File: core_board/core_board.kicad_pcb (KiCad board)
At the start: 2 copper layers, 27 x 60 mm, 36 parts, among them J1 Conn_01x13_Socket, J2 Conn_01x13_Socket, J3 Ignitor Output, J4 Micro_SD_Card, J5 Battery Input, J7 Connector 1, J8 Connector 2, U1 CPC1002N, U2 CPC1002N, U3 CPC1002N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

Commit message: Fixed connector compatibility with STEMMA QT and Qwiic
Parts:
- J7, J8: footprint Connector_Molex:Molex_PicoBlade_53047-0410_1x04_P1.25mm_Vertical -> G2Custom:JST_SH_BM04B-SRSS-TB_1x04-1MP_P1.00mm_Vertical-CUSTOM
- moved J7 1.46 mm to (118.8, 74.5)
- moved J8 0.98 mm to (118.8, 82.5)
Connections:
- J7 pad 1: +3.3V -> /SCL Inter Board
- J7 pad 2: /SCL Inter Board -> /SDA Inter Board
- J7 pad 3: /SDA Inter Board -> +3.3V
- J8 pad 1: +3.3V -> /SCL Inter Board
- J8 pad 2: /SCL Inter Board -> /SDA Inter Board
- J8 pad 3: /SDA Inter Board -> +3.3V
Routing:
- net +3.3V: track 117.7 -> 106.2 mm
- net /SDA Inter Board: track 22.2 -> 24.6 mm, vias 0 -> 2
- net GND: track 20.0 -> 21.5 mm, vias 19 -> 21
- net /SCL Inter Board: track 21.5 -> 22.0 mm

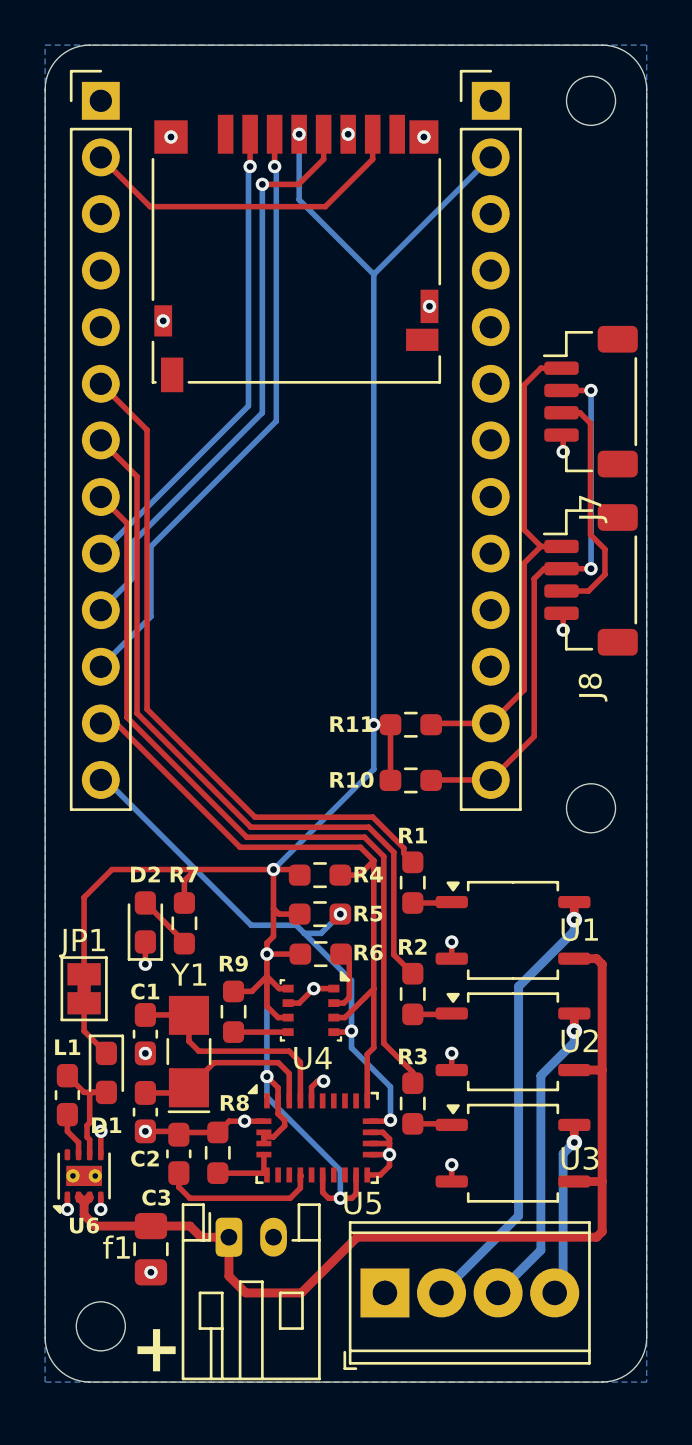
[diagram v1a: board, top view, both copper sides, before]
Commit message: Corrected DRC errors
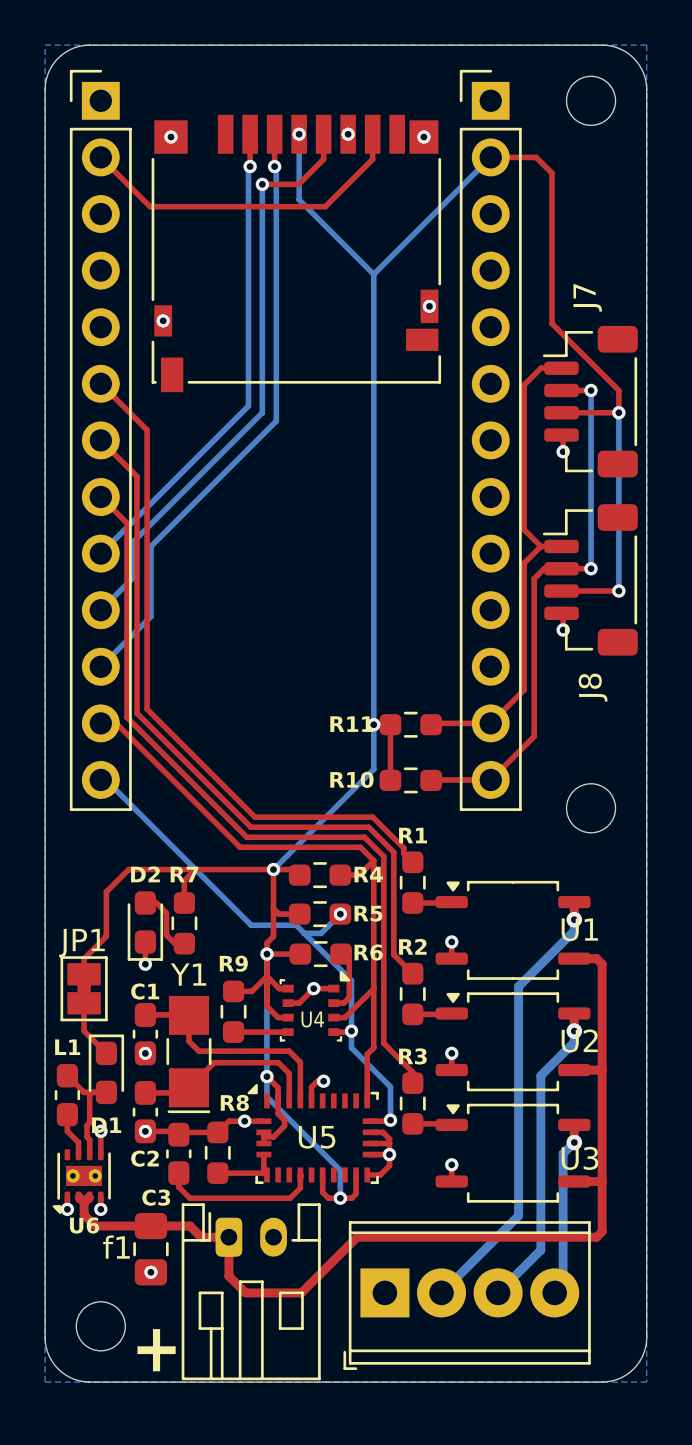
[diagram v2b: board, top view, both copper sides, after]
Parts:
- Y1: value 33.768kHz -> 32.768kHz
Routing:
- net +3.3V: track 106.2 -> 123.1 mm, vias 6 -> 8
- net Net-(D2-A): track 2.55 -> 3.09 mm
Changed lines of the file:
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@@
 			)
 		)
-		(property "Value" "33.768kHz"
+		(property "Value" "32.768kHz"
 			(at 0 -2 90)
 			(layer "F.Fab")
@@
 		(tags "lga land grid array")
 		(property "Reference" "U4"
-			(at 2.18125 -0.06875 180)
+			(at 0.43125 -0.06875 180)
 			(layer "F.SilkS")
 			(effects
 				(font
-					(size 1 1)
-					(thickness 0.15)
+					(size 0.7 0.6)
+					(thickness 0.125)
 				)
 			)
@@
 		(tags "LGA 28 5.2x3.8mm Pitch 0.5mm")
 		(property "Reference" "U5"
-			(at 2.04375 2.95625 0)
+			(at 0 0 0)
 			(layer "F.SilkS")
 			(effects
@@
 		(tags "connector JST SH vertical")
 		(property "Reference" "J7"
-			(at 4.75 0 90)
+			(at -4.75 0.25 90)
 			(layer "F.SilkS")
 			(effects
@@
 	)
 	(segment
-		(start 118.725 75.475)
-		(end 118.25 75)
-		(width 0.25)
-		(layer "F.Cu")
-		(net 1)
-	)
-	(segment
-		(start 118.725 80.475)
-		(end 118.725 75.475)
+		(start 100.5 96)
+		(end 101 95.5)
 		(width 0.25)
 		(layer "F.Cu")
@@
 	)
 	(segment
-		(start 97.25 95.5)
-		(end 99.922924 95.5)
+		(start 104.20625 101.64375)
+		(end 104.20625 100.29375)
 		(width 0.25)
 		(layer "F.Cu")
@@
 	)
 	(segment
-		(start 100.5 96)
-		(end 101 95.5)
+		(start 108.0135 110.25)
+		(end 108.20625 110.05725)
 		(width 0.25)
 		(layer "F.Cu")
@@
 	)
 	(segment
-		(start 104.20625 101.64375)
-		(end 104.20625 100.29375)
+		(start 114.25 63.54)
+		(end 116.29 63.54)
 		(width 0.25)
 		(layer "F.Cu")
@@
 	)
 	(segment
-		(start 108.0135 110.25)
-		(end 108.20625 110.05725)
+		(start 117 64.25)
+		(end 117 71)
 		(width 0.25)
 		(layer "F.Cu")
@@
 	)
 	(segment
-		(start 96 96.75)
-		(end 97.25 95.5)
+		(start 117 71)
+		(end 120 74)
 		(width 0.25)
 		(layer "F.Cu")
@@
 	)
 	(segment
-		(start 96 100.2)
-		(end 96 96.75)
-		(width 0.25)
-		(layer "F.Cu")
-		(net 1)
-	)
-	(segment
 		(start 104.20625 101.64375)
 		(end 104.70625 102.14375)
@@
 	)
 	(segment
+		(start 98 95.5)
+		(end 101 95.5)
+		(width 0.25)
+		(layer "F.Cu")
+		(net 1)
+	)
+	(segment
 		(start 105.70625 99.29375)
 		(end 104.20625 99.29375)
@@
 	)
 	(segment
-		(start 118.633884 83)
-		(end 119.375 82.258884)
+		(start 97 98.5)
+		(end 97 96.5)
 		(width 0.25)
 		(layer "F.Cu")
@@
 	)
 	(segment
-		(start 119.375 81.125)
-		(end 118.725 80.475)
+		(start 120 74)
+		(end 120 75)
 		(width 0.25)
 		(layer "F.Cu")
@@
 	)
 	(segment
+		(start 96 100.2)
+		(end 96 99.5)
+		(width 0.25)
+		(layer "F.Cu")
+		(net 1)
+	)
+	(segment
 		(start 105 106.7625)
 		(end 105 107)
@@
 	)
 	(segment
+		(start 117.425 75)
+		(end 120 75)
+		(width 0.25)
+		(layer "F.Cu")
+		(net 1)
+	)
+	(segment
 		(start 104.5 98.5)
 		(end 104.20625 98.79375)
@@
 	)
 	(segment
-		(start 117.425 83)
-		(end 118.633884 83)
+		(start 96 99.5)
+		(end 97 98.5)
 		(width 0.25)
 		(layer "F.Cu")
@@
 	)
 	(segment
+		(start 116.29 63.54)
+		(end 117 64.25)
+		(width 0.25)
+		(layer "F.Cu")
+		(net 1)
+	)
+	(segment
 		(start 104.70625 105.29375)
 		(end 104.20625 104.79375)
@@
 	)
 	(segment
-		(start 119.375 82.258884)
-		(end 119.375 81.125)
+		(start 104.06875 107.29375)
+		(end 104.06875 107.5)
 		(width 0.25)
 		(layer "F.Cu")
@@
 	)
 	(segment
-		(start 104.06875 107.29375)
-		(end 104.06875 107.5)
+		(start 117.425 83)
+		(end 120 83)
 		(width 0.25)
 		(layer "F.Cu")
@@
 	)
 	(segment
-		(start 99.922924 95.5)
-		(end 101 95.5)
+		(start 97 96.5)
+		(end 98 95.5)
 		(width 0.25)
 		(layer "F.Cu")
@@
 		(net 1)
 	)
-	(segment
-		(start 118.25 75)
-		(end 117.425 75)
-		(width 0.25)
-		(layer "F.Cu")
+	(via
+		(at 120 75)
+		(size 0.6)
+		(drill 0.3)
+		(layers "F.Cu" "B.Cu")
 		(net 1)
 	)
@@
 		(net 1)
 	)
+	(via
+		(at 120 83)
+		(size 0.6)
+		(drill 0.3)
+		(layers "F.Cu" "B.Cu")
+		(net 1)
+	)
 	(segment
 		(start 107.5 109)
@@
 	)
 	(segment
+		(start 120 83)
+		(end 120 75)
+		(width 0.25)
+		(layer "B.Cu")
+		(net 1)
+	)
+	(segment
 		(start 104.5 95.5)
 		(end 109 91)
@@
 	)
 	(segment
-		(start 100.5 98.75)
-		(end 100.5 98.825)
+		(start 99.7 97.45)
+		(end 99.7 98.45)
 		(width 0.25)
 		(layer "F.Cu")
@@
 	(segment
 		(start 98.75 97)
-		(end 100.5 98.75)
+		(end 99.25 97)
+		(width 0.25)
+		(layer "F.Cu")
+		(net 48)
+	)
+	(segment
+		(start 100.075 98.825)
+		(end 100.5 98.825)
+		(width 0.25)
+		(layer "F.Cu")
+		(net 48)
+	)
+	(segment
+		(start 99.25 97)
+		(end 99.7 97.45)
+		(width 0.25)
+		(layer "F.Cu")
+		(net 48)
+	)
+	(segment
+		(start 99.7 98.45)
+		(end 100.075 98.825)
 		(width 0.25)
 		(layer "F.Cu")
@@
 	)
 	(zone
+		(net 46)
+		(net_name "GND")
+		(layer "F.Cu")
+		(name "$teardrop_padvia$")
+		(hatch full 0.1)
+		(priority 30001)
+		(attr
+			(teardrop
+				(type padvia)
+			)
+		)
+		(connect_pads yes
+			(clearance 0)
+		)
+		(min_thickness 0.0254)
+		(filled_areas_thickness no)
+		(fill yes
+			(thermal_gap 0.5)
+			(thermal_bridge_width 0.5)
+			(island_removal_mode 1)
+			(island_area_min 10)
+		)
+		(polygon
+			(pts
+				(xy 96.875 110.2) (xy 96.625 110.2) (xy 96.472836 110.635195) (xy 96.75 110.751) (xy 97.027164 110.635195)
+			)
+		)
+	)
+	(zone
+		(net 46)
+		(net_name "GND")
+		(layer "F.Cu")
+		(name "$teardrop_padvia$")
+		(hatch full 0.1)
+		(priority 30002)
+		(attr
+			(teardrop
+				(type padvia)
+			)
+		)
+		(connect_pads yes
+			(clearance 0)
+		)
+		(min_thickness 0.0254)
+		(filled_areas_thickness no)
+		(fill yes
+			(thermal_gap 0.5)
+			(thermal_bridge_width 0.5)
+			(island_removal_mode 1)
+			(island_area_min 10)
+		)
+		(polygon
+			(pts
+				(xy 95.375 110.2) (xy 95.125 110.2) (xy 94.972836 110.635195) (xy 95.25 110.751) (xy 95.527164 110.635195)
+			)
+		)
+	)
+	(zone
